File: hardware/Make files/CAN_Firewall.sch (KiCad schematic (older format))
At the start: 31 parts, among them J1 DB9, J2 DB9, U1 MCP2551-I/SN, U2 MCP2551-I/SN, U3 MC78M05CDT, U4 AT32UC3C, U5 SMF05

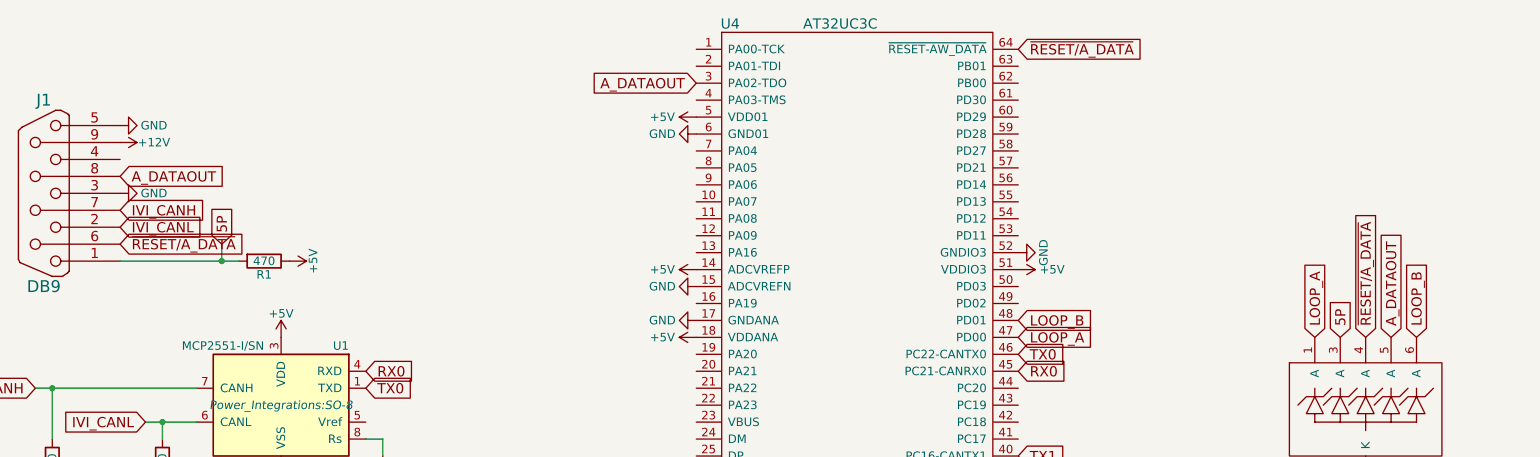
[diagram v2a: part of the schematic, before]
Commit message: exploring the fixes for the proto
made a rudimentary design to copy when building the CBFW proto, as it
requires modifications.
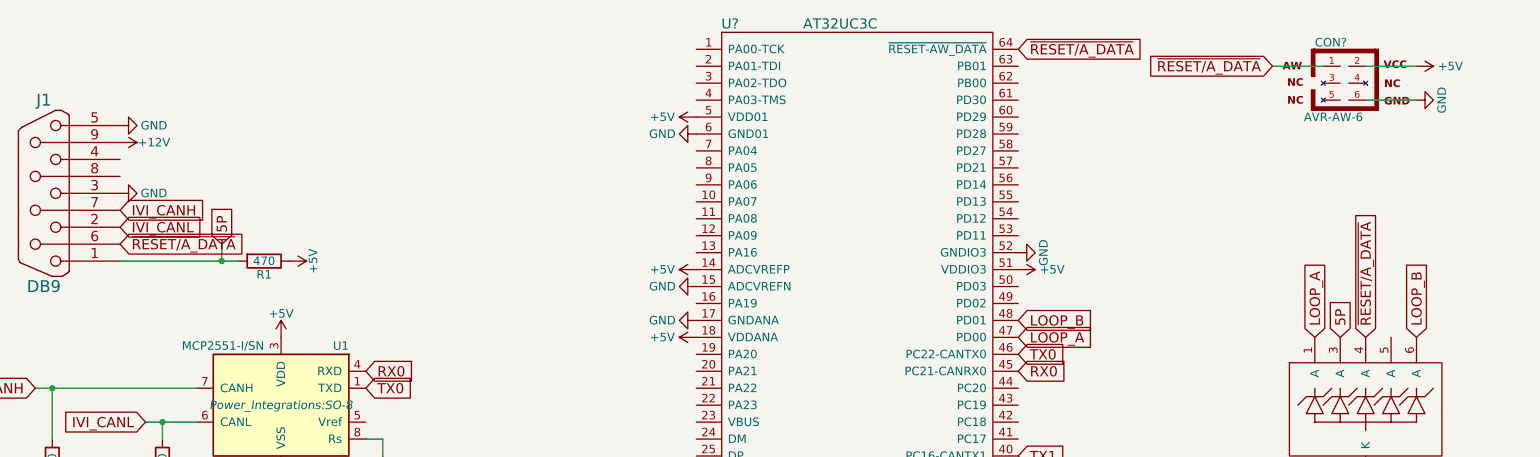
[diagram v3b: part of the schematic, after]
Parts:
- removed U4: AT32UC3C, Housings_QFP:TQFP-64_10x10mm_Pitch0.5mm, symbol AT32UC3C
- added CON?: AVR-AW-6, AVR-AW-6, symbol AVR-AW-6
- added U?: AT32UC3C, symbol AT32UC3C
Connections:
- net +5V: now also CON?.2, U?.14 (ADCVREFP), U?.18 (VDDANA), U?.27 (VDDIN_5), U?.35 (VDDIO2), U?.5 (VDD01), U?.51 (VDDIO3)
- net GND: now also CON?.6, U?.15 (ADCVREFN), U?.17 (GNDANA), U?.26 (GNDPLL), U?.30 (GNDCORE), U?.36 (GNDIO2), U?.52 (GNDIO3), U?.6 (GND01)
- net LOOP_A: now also U?.47 (PD00)
- net LOOP_B: now also U?.48 (PD01)
- net RX0: now also U?.45 (PC21-CANRX0)
- net RX1: now also U?.39 (PC15-CANRX1)
- net TX0: now also U?.46 (PC22-CANTX0)
- net TX1: now also U?.40 (PC16-CANTX1)
- net ~RESET/A_DATA: now also CON?.1, U?.64 (~RESET-AW_DATA)
- net at C13.1: now also U?.29 (VDDCORE)
- net at C12.1: now also U?.28 (VDDIN_33)
- net A_DATAOUT: no longer names the net of U5.5 (A)
- net A_DATAOUT: no longer J1.8 (P8)
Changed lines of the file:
@@
 LIBS:contrib
 LIBS:valves
+LIBS:CUSTOM_KICAD_PART
 LIBS:CAN_Firewall-cache
 EELAYER 25 0
@@
 Text GLabel 1800 2200 2    60   Input ~ 0
 ~RESET/A_DATA
-Text GLabel 1800 1800 2    60   Input ~ 0
-A_DATAOUT
 $Comp
 L R R1
@@
 Text GLabel 7100 1050 2    60   Input ~ 0
 ~RESET/A_DATA
-Text GLabel 5200 1250 0    60   Input ~ 0
-A_DATAOUT
-$Comp
-L AT32UC3C U4
-U 1 1 55CCDC98
-P 6200 2600
-F 0 "U4" H 5400 4300 60  0000 C CNN
-F 1 "AT32UC3C" H 6050 4300 60  0000 C CNN
-F 2 "Housings_QFP:TQFP-64_10x10mm_Pitch0.5mm" H 6200 2600 60  0001 C CNN
-F 3 "" H 6200 2600 60  0000 C CNN
-	1    6200 2600
-	1    0    0    -1
-$EndComp
 $Comp
 L GND #PWR028
@@
 Text GLabel 9150 2750 1    60   Input ~ 0
 ~RESET/A_DATA
-Text GLabel 9300 2750 1    60   Input ~ 0
-A_DATAOUT
 Text GLabel 9450 2750 1    60   Input ~ 0
 LOOP_B
@@
 Wire Wire Line
 	2100 5350 2300 5350
+$Comp
+L AT32UC3C U?
+U 1 1 55D650EA
+P 6200 2600
+F 0 "U?" H 5400 4300 60  0000 C CNN
+F 1 "AT32UC3C" H 6050 4300 60  0000 C CNN
+F 2 "" H 6200 2600 60  0000 C CNN
+F 3 "" H 6200 2600 60  0000 C CNN
+	1    6200 2600
+	1    0    0    -1
+$EndComp
+$Comp
+L AVR-AW-6 CON?
+U 1 1 55D64F4F
+P 9050 1250
+F 0 "CON?" H 8945 1490 50  0000 C CNN
+F 1 "AVR-AW-6" H 8785 1020 50  0000 L BNN
+F 2 "AVR-AW-6" V 8530 1290 50  0001 C CNN
+F 3 "" H 9025 1250 60  0000 C CNN
+	1    9050 1250
+	1    0    0    -1
+$EndComp
+Text GLabel 8600 1150 0    60   Input ~ 0
+~RESET/A_DATA
+Wire Wire Line
+	8600 1150 8900 1150
+$Comp
+L GND #PWR?
+U 1 1 55D65104
+P 9450 1350
+F 0 "#PWR?" H 9450 1100 50  0001 C CNN
+F 1 "GND" H 9450 1200 50  0000 C CNN
+F 2 "" H 9450 1350 60  0000 C CNN
+F 3 "" H 9450 1350 60  0000 C CNN
+	1    9450 1350
+	0    -1   -1   0
+$EndComp
+$Comp
+L +5V #PWR?
+U 1 1 55D6516F
+P 9450 1150
+F 0 "#PWR?" H 9450 1000 50  0001 C CNN
+F 1 "+5V" V 9450 1350 50  0000 C CNN
+F 2 "" H 9450 1150 60  0000 C CNN
+F 3 "" H 9450 1150 60  0000 C CNN
+	1    9450 1150
+	0    1    1    0
+$EndComp
+Wire Wire Line
+	9450 1150 9150 1150
+Wire Wire Line
+	9150 1350 9450 1350
 $EndSCHEMATC
